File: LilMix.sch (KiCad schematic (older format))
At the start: 53 parts, among them J1_L1 MONO, J1_R1 MONO, J2_L1 MONO, J2_R1 MONO, J3 STEREO, J4 MONO, J5 MONO, J6 STEREO, U1 TL074, U2 NE5532

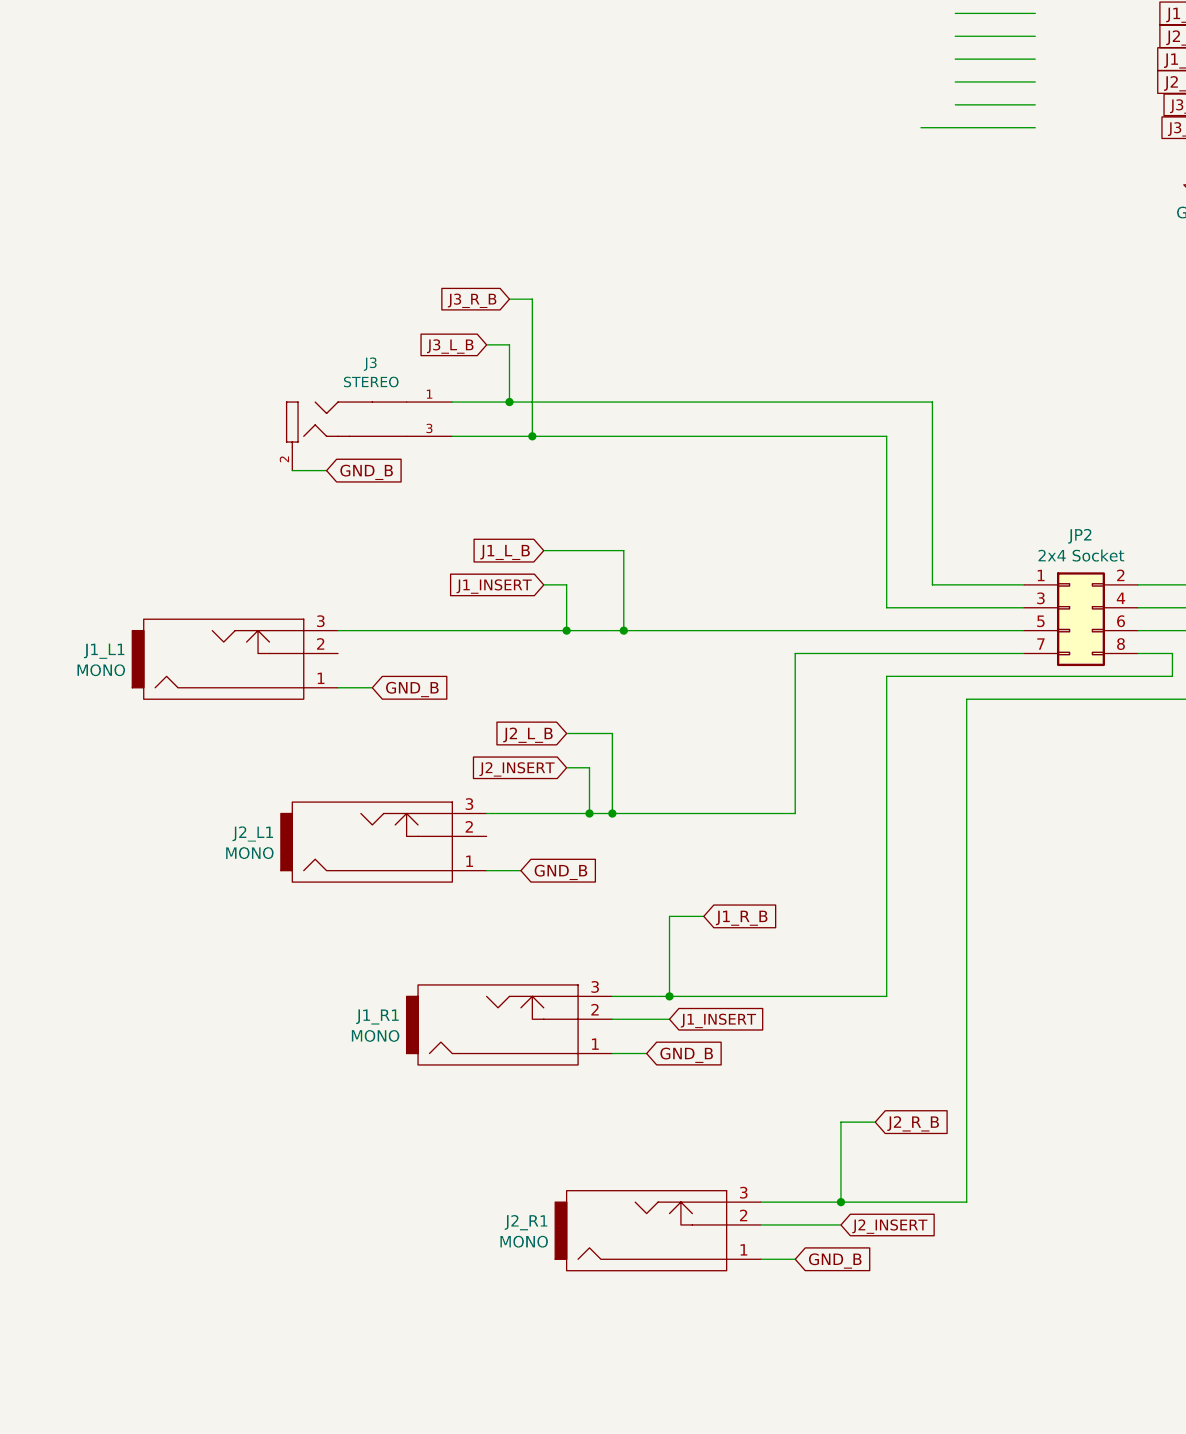
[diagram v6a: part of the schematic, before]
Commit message: Added dc filtering capacitors to inputs
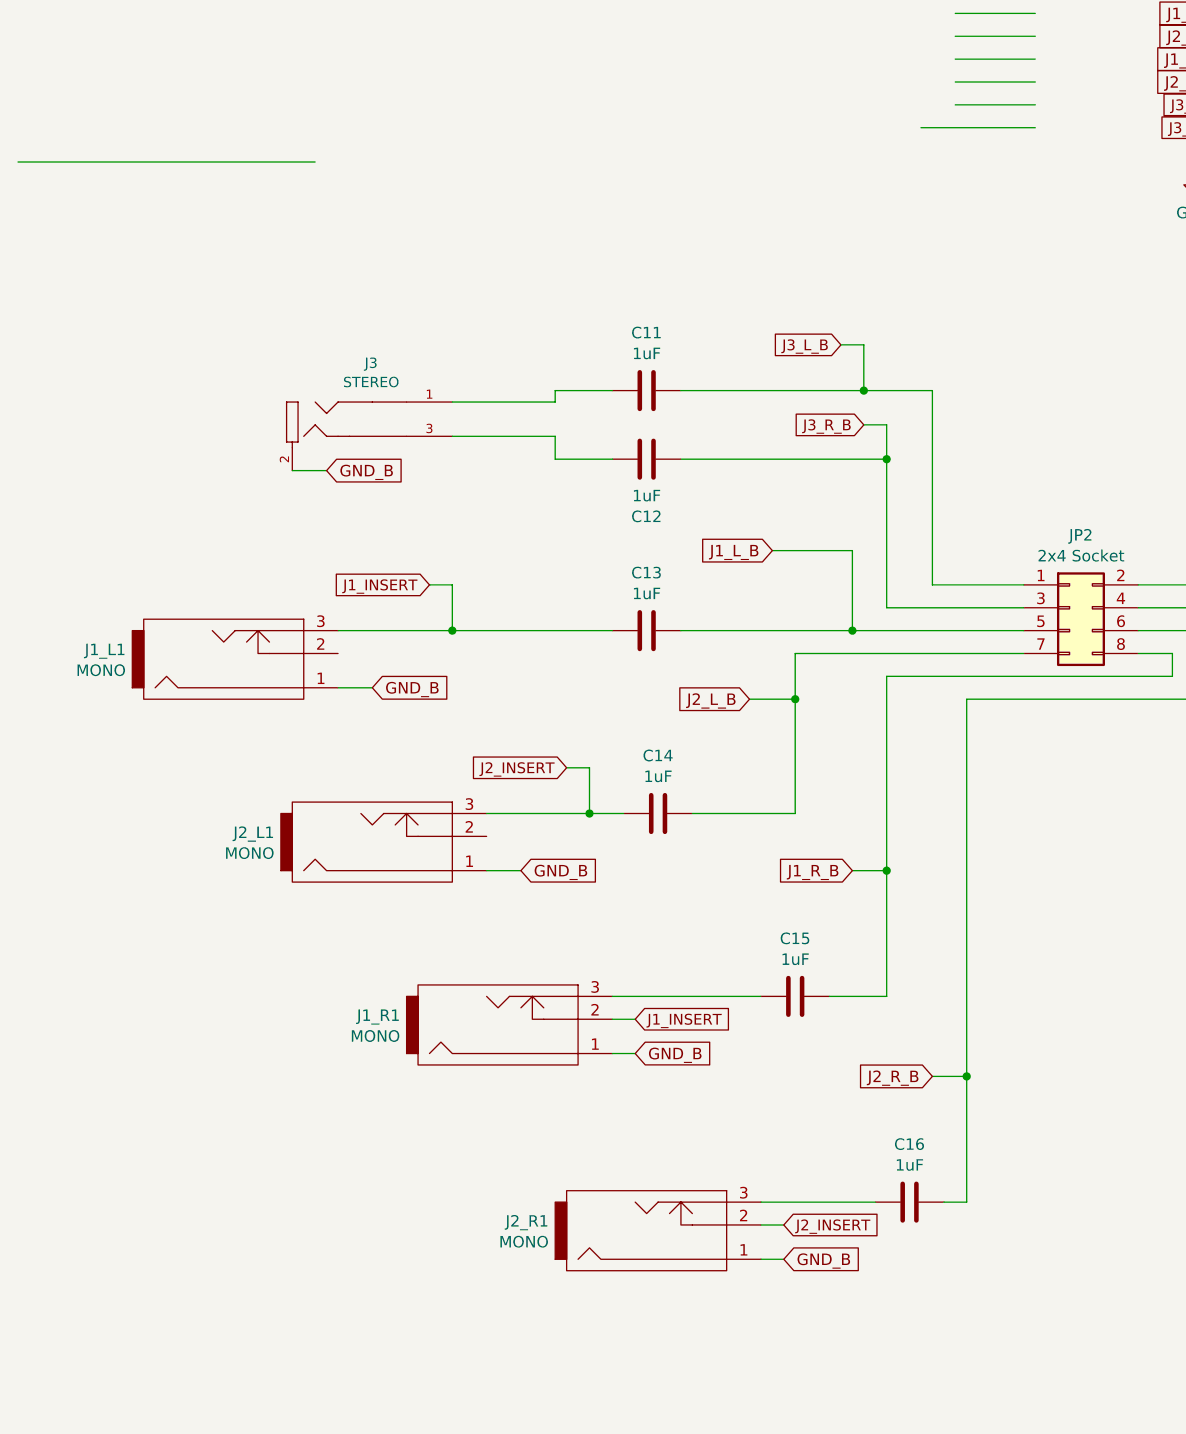
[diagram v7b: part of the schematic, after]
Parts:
- added C11, C12, C13, C14, C15, C16: 1uF, Capacitor_THT:C_Rect_L7.0mm_W4.5mm_P5.00mm, symbol 4ms-passives:C
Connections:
- wire segments 281 -> 288
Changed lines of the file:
@@
 $EndComp
 Wire Wire Line
-	-5200 5850 -4850 5850
-Wire Wire Line
-	-6300 2100 -6400 2100
-Wire Wire Line
-	-5850 5050 -5600 5050
-Wire Wire Line
-	-5850 4950 -5600 4950
-Text GLabel -5600 5050 2    47   Input ~ 0
+	-4750 2100 -4850 2100
+Wire Wire Line
+	-5850 5050 -5750 5050
+Text GLabel -5750 5050 2    47   Input ~ 0
 J1_INSERT
 Wire Wire Line
@@
 	0    1    -1   0
 $EndComp
-Text GLabel -6400 2100 0    47   Input ~ 0
+Text GLabel -4850 2100 0    47   Input ~ 0
 J3_L_B
-Text GLabel -4850 5950 2    47   Input ~ 0
+Text GLabel -5100 5950 2    47   Input ~ 0
 J2_INSERT
 Wire Wire Line
-	-6050 3150 -6050 3350
-Wire Wire Line
-	-6150 3150 -6050 3150
-Text GLabel -6150 3150 0    47   Input ~ 0
+	-6550 3150 -6550 3350
+Wire Wire Line
+	-6650 3150 -6550 3150
+Text GLabel -6650 3150 0    47   Input ~ 0
 J1_INSERT
 Wire Wire Line
@@
 Text Notes 6300 7250 0    354  ~ 0
 LilMix Main
-Text GLabel -6150 3000 0    50   Input ~ 0
+Text GLabel -5150 3000 0    50   Input ~ 0
 J1_L_B
 Wire Wire Line
-	-6150 3000 -5800 3000
-Wire Wire Line
-	-5800 3000 -5800 3350
-Connection ~ -5800 3350
-Wire Wire Line
-	-5800 3350 -4050 3350
+	-5150 3000 -4800 3000
+Wire Wire Line
+	-4800 3000 -4800 3350
 Text GLabel 1600 1250 0    50   Input ~ 0
 J1_L_A
@@
 Wire Wire Line
 	-5050 3450 -4050 3450
-Connection ~ -5850 4150
-Wire Wire Line
-	-5850 4150 -5050 4150
-Wire Wire Line
-	-5050 4150 -5050 3450
 Wire Wire Line
 	-6400 4400 -6250 4400
@@
 GND_B
 Wire Wire Line
-	-5850 3800 -5850 4150
-Wire Wire Line
-	-6050 3800 -5850 3800
-Text GLabel -6050 3800 0    50   Input ~ 0
+	-5250 3650 -5050 3650
+Text GLabel -5250 3650 0    50   Input ~ 0
 J2_L_B
 $Comp
@@
 Wire Wire Line
 	-5950 3950 -5950 4150
-Connection ~ -5950 4150
-Wire Wire Line
-	-5950 4150 -5850 4150
-Wire Wire Line
-	-5850 5200 -5700 5200
-Text GLabel -5700 5200 2    50   Input ~ 0
+Wire Wire Line
+	-5850 5200 -5750 5200
+Text GLabel -5750 5200 2    50   Input ~ 0
 GND_B
 Wire Wire Line
-	-5200 5950 -4850 5950
-Wire Wire Line
-	-5200 6100 -5050 6100
-Text GLabel -5050 6100 2    50   Input ~ 0
+	-5200 5950 -5100 5950
+Wire Wire Line
+	-5200 6100 -5100 6100
+Text GLabel -5100 6100 2    50   Input ~ 0
 GND_B
-Wire Wire Line
-	-5600 4600 -5600 4950
-Wire Wire Line
-	-5450 4600 -5600 4600
-Text GLabel -5450 4600 2    50   Input ~ 0
+Text GLabel -4800 4400 0    50   Input ~ 0
 J1_R_B
 Wire Wire Line
-	-4850 5500 -4850 5850
-Wire Wire Line
-	-4700 5500 -4850 5500
-Text GLabel -4700 5500 2    50   Input ~ 0
+	-4450 5300 -4300 5300
+Text GLabel -4450 5300 0    50   Input ~ 0
 J2_R_B
-Connection ~ -4850 5850
-Connection ~ -5600 4950
-Wire Wire Line
-	-4650 3550 -4650 4950
-Wire Wire Line
-	-5600 4950 -4650 4950
-Wire Wire Line
-	-4300 5850 -4300 3650
-Wire Wire Line
-	-4850 5850 -4300 5850
-Wire Wire Line
-	-6300 2350 -6300 2100
-Wire Wire Line
-	-6200 1900 -6300 1900
-Text GLabel -6300 1900 0    47   Input ~ 0
+Wire Wire Line
+	-4650 3550 -4650 4400
+Wire Wire Line
+	-4650 2450 -4750 2450
+Text GLabel -4750 2450 0    47   Input ~ 0
 J3_R_B
-Wire Wire Line
-	-6200 1900 -6200 2500
 Text GLabel -2800 750  2    50   Input ~ 0
 J2_L_B
@@
 J3_R_A
 Wire Wire Line
-	-6550 2350 -6300 2350
-Wire Wire Line
-	-6300 2350 -4450 2350
-Wire Wire Line
-	-4450 2350 -4450 3150
-Wire Wire Line
 	-4450 3150 -4050 3150
-Connection ~ -6300 2350
 Wire Wire Line
 	-4050 3250 -4650 3250
-Wire Wire Line
-	-4650 3250 -4650 2500
-Wire Wire Line
-	-4650 2500 -6200 2500
-Wire Wire Line
-	-6550 2500 -6200 2500
-Connection ~ -6200 2500
 Text GLabel -7100 2650 2    50   Input ~ 0
 GND_B
@@
 Wire Wire Line
 	-3150 3150 -3150 3250
-Connection ~ -6050 3350
-Wire Wire Line
-	-6050 3350 -5800 3350
-Wire Wire Line
-	-7050 3350 -6050 3350
+Wire Wire Line
+	-7050 3350 -6550 3350
 $Comp
 L 4ms-headers:Conn_02x04_Odd_Even JP2
@@
 Wire Wire Line
 	4350 5650 4250 5650
+$Comp
+L 4ms-passives:C C11
+U 1 1 5E6EE0E9
+P -5700 2300
+F 0 "C11" V -5952 2300 50  0000 C CNN
+F 1 "1uF" V -5861 2300 50  0000 C CNN
+F 2 "Capacitor_THT:C_Rect_L7.0mm_W4.5mm_P5.00mm" H -5662 2150 50  0001 C CNN
+F 3 "" H -5700 2300 50  0001 C CNN
+	1    -5700 2300
+	0    1    1    0
+$EndComp
+Wire Wire Line
+	-4650 2450 -4650 2600
+$Comp
+L 4ms-passives:C C12
+U 1 1 5E77E136
+P -5700 2600
+F 0 "C12" V -5952 2600 50  0000 C CNN
+F 1 "1uF" V -5861 2600 50  0000 C CNN
+F 2 "Capacitor_THT:C_Rect_L7.0mm_W4.5mm_P5.00mm" H -5662 2450 50  0001 C CNN
+F 3 "" H -5700 2600 50  0001 C CNN
+	1    -5700 2600
+	0    -1   -1   0
+$EndComp
+Wire Wire Line
+	-6550 2350 -6100 2350
+Wire Wire Line
+	-6100 2350 -6100 2300
+Wire Wire Line
+	-6100 2300 -5850 2300
+Wire Wire Line
+	-5550 2300 -4750 2300
+Connection ~ -4750 2300
+Wire Wire Line
+	-4750 2300 -4750 2100
+Wire Wire Line
+	-4450 2300 -4750 2300
+Wire Wire Line
+	-4450 2300 -4450 3150
+Wire Wire Line
+	-6550 2500 -6100 2500
+Wire Wire Line
+	-6100 2500 -6100 2600
+Wire Wire Line
+	-6100 2600 -5850 2600
+Wire Wire Line
+	-5550 2600 -4650 2600
+Connection ~ -4650 2600
+Wire Wire Line
+	-4650 2600 -4650 3250
+Wire Wire Line
+	-4800 3350 -4050 3350
+Wire Wire Line
+	-8450 1300 -7150 1300
+$Comp
+L 4ms-passives:C C13
+U 1 1 5E96373C
+P -5700 3350
+F 0 "C13" V -5952 3350 50  0000 C CNN
+F 1 "1uF" V -5861 3350 50  0000 C CNN
+F 2 "Capacitor_THT:C_Rect_L7.0mm_W4.5mm_P5.00mm" H -5662 3200 50  0001 C CNN
+F 3 "" H -5700 3350 50  0001 C CNN
+	1    -5700 3350
+	0    1    1    0
+$EndComp
+Wire Wire Line
+	-4800 3350 -5550 3350
+Connection ~ -4800 3350
+Wire Wire Line
+	-5850 3350 -6550 3350
+Connection ~ -6550 3350
+$Comp
+L 4ms-passives:C C14
+U 1 1 5EA7A2EC
+P -5650 4150
+F 0 "C14" V -5902 4150 50  0000 C CNN
+F 1 "1uF" V -5811 4150 50  0000 C CNN
+F 2 "Capacitor_THT:C_Rect_L7.0mm_W4.5mm_P5.00mm" H -5612 4000 50  0001 C CNN
+F 3 "" H -5650 4150 50  0001 C CNN
+	1    -5650 4150
+	0    1    1    0
+$EndComp
+Wire Wire Line
+	-5050 3650 -5050 3450
+Wire Wire Line
+	-5500 4150 -5050 4150
+Wire Wire Line
+	-5050 4150 -5050 3650
+Connection ~ -5050 3650
+Wire Wire Line
+	-5800 4150 -5950 4150
+Connection ~ -5950 4150
+$Comp
+L 4ms-passives:C C15
+U 1 1 5EB9648D
+P -5050 4950
+F 0 "C15" V -5302 4950 50  0000 C CNN
+F 1 "1uF" V -5211 4950 50  0000 C CNN
+F 2 "Capacitor_THT:C_Rect_L7.0mm_W4.5mm_P5.00mm" H -5012 4800 50  0001 C CNN
+F 3 "" H -5050 4950 50  0001 C CNN
+	1    -5050 4950
+	0    1    1    0
+$EndComp
+Wire Wire Line
+	-4650 4950 -4900 4950
+Wire Wire Line
+	-5200 4950 -5850 4950
+Connection ~ -4300 5300
+Wire Wire Line
+	-4800 4400 -4650 4400
+Connection ~ -4650 4400
+Wire Wire Line
+	-4650 4400 -4650 4950
+Wire Wire Line
+	-4300 3650 -4300 5300
+$Comp
+L 4ms-passives:C C16
+U 1 1 5ED55C6A
+P -4550 5850
+F 0 "C16" V -4802 5850 50  0000 C CNN
+F 1 "1uF" V -4711 5850 50  0000 C CNN
+F 2 "Capacitor_THT:C_Rect_L7.0mm_W4.5mm_P5.00mm" H -4512 5700 50  0001 C CNN
+F 3 "" H -4550 5850 50  0001 C CNN
+	1    -4550 5850
+	0    1    1    0
+$EndComp
+Wire Wire Line
+	-5200 5850 -4700 5850
+Wire Wire Line
+	-4400 5850 -4300 5850
+Wire Wire Line
+	-4300 5300 -4300 5850
 $EndSCHEMATC

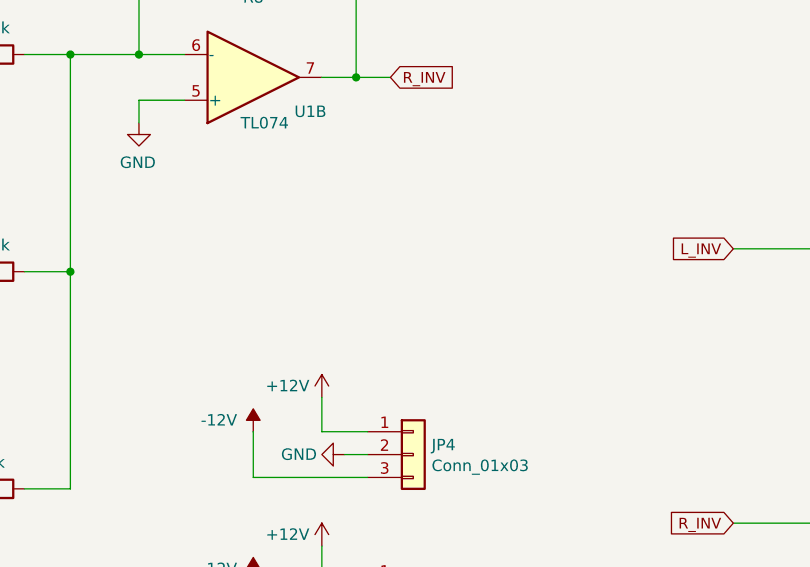
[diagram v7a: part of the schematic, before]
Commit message: Added another +12v socket header. Initial routing completed
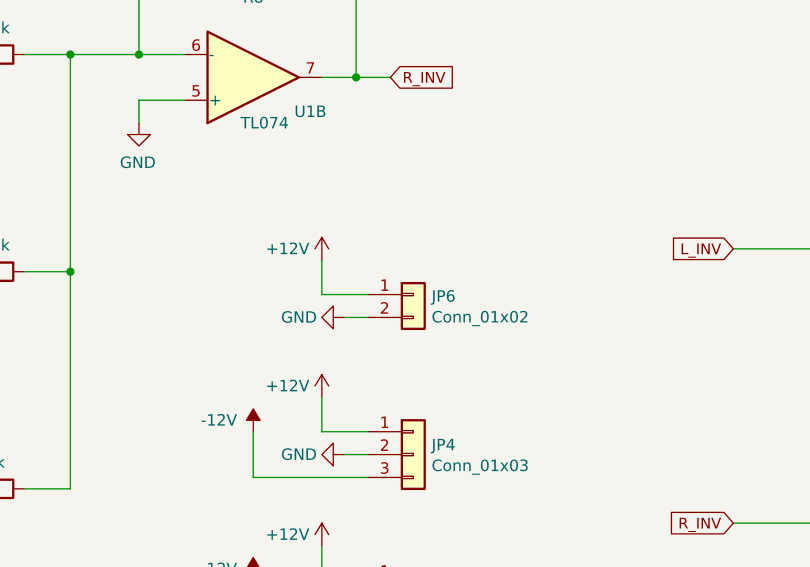
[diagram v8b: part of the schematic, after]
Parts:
- added JP6: Conn_01x02, Connector_PinSocket_2.54mm:PinSocket_1x02_P2.54mm_Vertical, symbol 4ms-headers:Conn_01x02
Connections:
- wire segments 288 -> 291
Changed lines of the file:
@@
 Wire Wire Line
 	-4300 5300 -4300 5850
+$Comp
+L 4ms-headers:Conn_01x02 JP6
+U 1 1 5EE41611
+P 4550 4950
+F 0 "JP6" H 4630 4942 50  0000 L CNN
+F 1 "Conn_01x02" H 4630 4851 50  0000 L CNN
+F 2 "Connector_PinSocket_2.54mm:PinSocket_1x02_P2.54mm_Vertical" H 4550 4950 50  0001 C CNN
+F 3 "~" H 4550 4950 50  0001 C CNN
+	1    4550 4950
+	1    0    0    -1
+$EndComp
+Wire Wire Line
+	4150 4950 4350 4950
+Wire Wire Line
+	4150 4950 4150 4800
+$Comp
+L power:+12V #PWR0132
+U 1 1 5EE433FE
+P 4150 4800
+F 0 "#PWR0132" H 4150 4650 50  0001 C CNN
+F 1 "+12V" H 4300 4850 50  0000 C CNN
+F 2 "" H 4150 4800 50  0001 C CNN
+F 3 "" H 4150 4800 50  0001 C CNN
+	1    4150 4800
+	-1   0    0    -1
+$EndComp
+$Comp
+L 4ms-power:GND #PWR0133
+U 1 1 5EE43408
+P 4250 5050
+F 0 "#PWR0133" H 4250 4800 50  0001 C CNN
+F 1 "GND" V 4250 4850 50  0000 C CNN
+F 2 "" H 4250 5050 50  0001 C CNN
+F 3 "" H 4250 5050 50  0001 C CNN
+	1    4250 5050
+	0    1    1    0
+$EndComp
+Wire Wire Line
+	4350 5050 4250 5050
 $EndSCHEMATC
